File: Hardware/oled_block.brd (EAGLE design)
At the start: 30.5 x 44.5 mm, 35 parts, among them J1 EDISON_CONNECTOR_FULLMOUNTING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

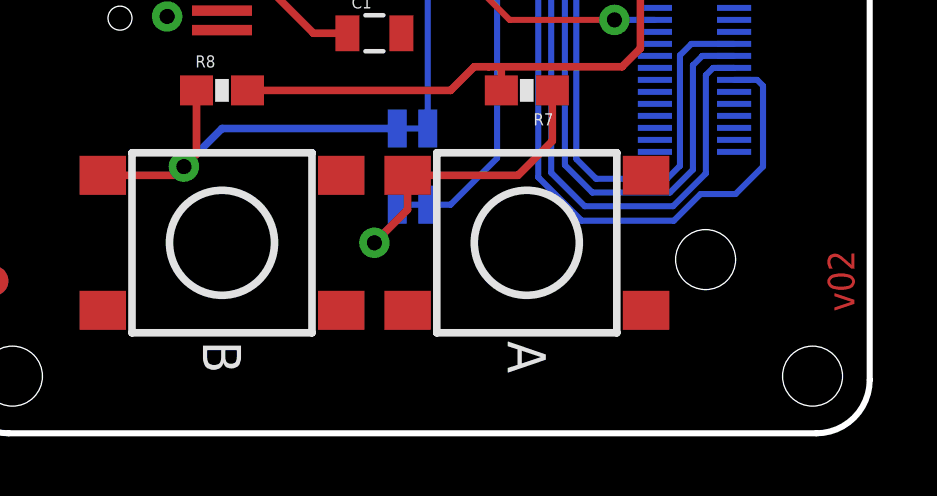
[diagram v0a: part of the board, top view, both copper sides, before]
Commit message: cleaning up some silk (v10)
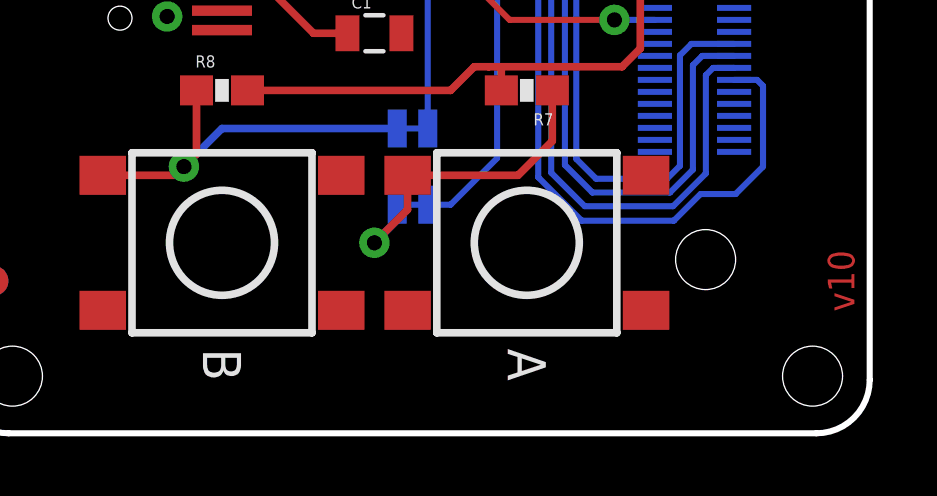
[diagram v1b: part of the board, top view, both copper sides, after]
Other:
- board text added: "v10"
- board text removed: "v02"

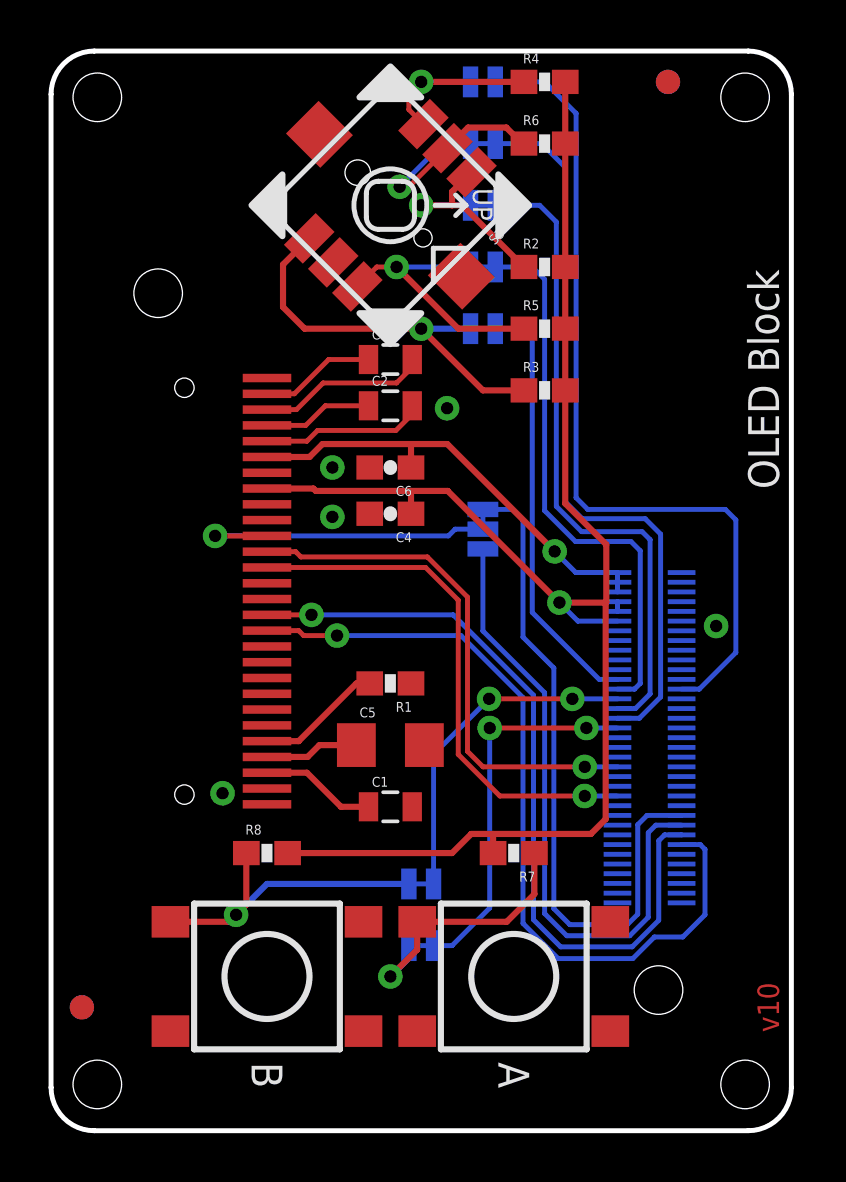
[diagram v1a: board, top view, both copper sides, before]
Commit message: Fixing button package. Silk fixes
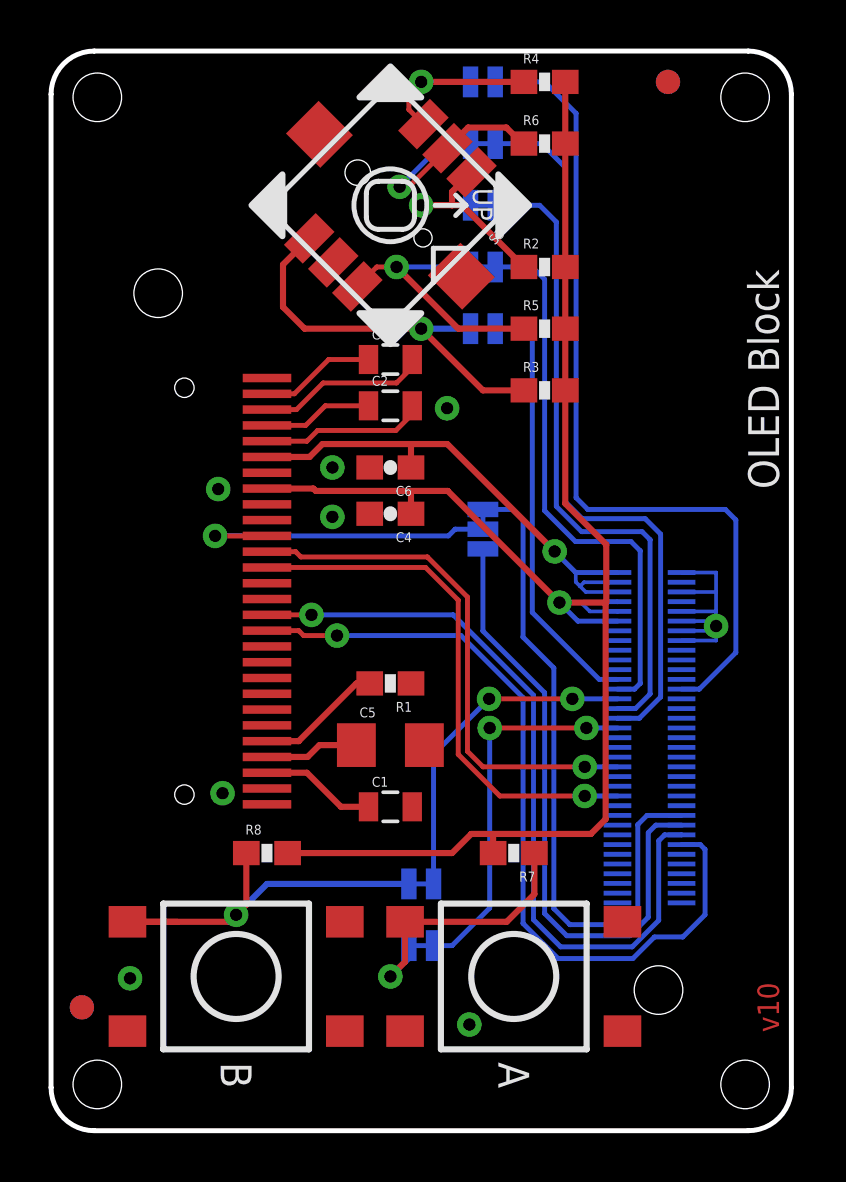
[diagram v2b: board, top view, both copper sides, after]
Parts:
- moved S2 1.27 mm to (7.62, 6.35)
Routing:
- net GND: track 0.00 -> 11.5 mm, vias 5 -> 8
- net BUT_B: track 14.0 -> 17.5 mm
- net VSYS: track 18.6 -> 21.7 mm
- net 3.3V: track 0.60 -> 3.12 mm
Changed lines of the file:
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@@
 <drawing>
 <settings>
-<setting alwaysvectorfont="no"/>
+<setting alwaysvectorfont="yes"/>
 <setting verticaltext="up"/>
 </settings>
-<grid distance="0.05" unitdist="inch" unit="inch" style="lines" multiple="1" display="yes" altdistance="0.005" altunitdist="inch" altunit="inch"/>
+<grid distance="0.025" unitdist="inch" unit="inch" style="lines" multiple="1" display="yes" altdistance="0.005" altunitdist="inch" altunit="inch"/>
 <layers>
 <layer number="1" name="Top" color="4" fill="1" visible="yes" active="yes"/>
@@
 <layer number="47" name="Measures" color="7" fill="1" visible="no" active="yes"/>
 <layer number="48" name="Document" color="7" fill="1" visible="no" active="yes"/>
-<layer number="49" name="Reference" color="7" fill="1" visible="yes" active="yes"/>
+<layer number="49" name="Reference" color="7" fill="1" visible="no" active="yes"/>
 <layer number="50" name="dxf" color="7" fill="1" visible="no" active="no"/>
 <layer number="51" name="tDocu" color="6" fill="1" visible="yes" active="yes"/>
@@
 <rectangle x1="22.098" y1="26.162" x2="30.48" y2="44.45" layer="42" rot="R180"/>
 <rectangle x1="22.098" y1="26.162" x2="30.48" y2="44.45" layer="41" rot="R180"/>
-<text x="29.21" y="6.35" size="1.016" layer="22" font="vector" ratio="15" rot="MR90" align="center">4xM2.0</text>
+<text x="29.21" y="6.35" size="1.016" layer="22" font="vector" ratio="15" rot="SMR270" align="center">4xM2.0</text>
 <text x="19.05" y="24.765" size="0.889" layer="22" font="vector" ratio="15" rot="MR90" align="bottom-center">!CS!</text>
 <text x="17.78" y="23.2664" size="0.889" layer="22" font="vector" ratio="15" rot="MR90" align="center-right">FS0</text>
 <text x="17.78" y="26.4414" size="0.889" layer="22" font="vector" ratio="15" rot="MR90" align="center-left">FS1</text>
 <text x="19.05" y="2.286" size="1.27" layer="21" font="vector" ratio="15" rot="SR270" align="center">A</text>
-<text x="8.89" y="2.286" size="1.27" layer="21" font="vector" ratio="15" rot="SR270" align="center">B</text>
+<text x="7.62" y="2.286" size="1.27" layer="21" font="vector" ratio="15" rot="SR270" align="center">B</text>
 <text x="29.972" y="26.416" size="1.27" layer="21" font="vector" ratio="15" rot="SR90">OLED Block</text>
 <text x="16.51" y="43.18" size="0.889" layer="22" font="vector" ratio="15" rot="MR180" align="center-right">L</text>
@@
 <attribute name="PROD_ID" value="SWCH-11966" x="19.05" y="6.35" size="1.778" layer="27" rot="R180" display="off"/>
 </element>
-<element name="S2" library="SparkFun-Electromechanical" package="TACTILE_SWITCH_TALL" value="Button B" x="8.89" y="6.35" rot="R180">
-<attribute name="PROD_ID" value="SWCH-11966" x="8.89" y="6.35" size="1.778" layer="27" rot="R180" display="off"/>
+<element name="S2" library="SparkFun-Electromechanical" package="TACTILE_SWITCH_TALL" value="Button B" x="7.62" y="6.35" rot="R180">
+<attribute name="PROD_ID" value="SWCH-11966" x="7.62" y="6.35" size="1.778" layer="27" rot="R180" display="off"/>
 </element>
 <element name="S3" library="SparkFun-Electromechanical" package="JOYSTICK_MINI" value="" x="13.97" y="38.1" rot="R225"/>
@@
 <signals>
 <signal name="GND">
-<polygon width="0.2032" layer="16" spacing="0.254" isolate="0.1524" orphans="yes" rank="6">
+<polygon width="0.1778" layer="16" spacing="0.254" isolate="0.1524" orphans="yes" rank="6">
 <vertex x="30.48" y="42.672"/>
 <vertex x="30.48" y="1.778" curve="-90"/>
@@
 <vertex x="28.702" y="44.45" curve="-90"/>
 </polygon>
-<polygon width="0.2032" layer="1" spacing="0.254" isolate="0.1524" orphans="yes" rank="6">
+<polygon width="0.1778" layer="1" spacing="0.254" isolate="0.1524" orphans="yes" rank="6">
 <vertex x="30.48" y="1.728" curve="-90"/>
 <vertex x="28.752" y="0"/>
@@
 <via x="7.0612" y="13.8938" extent="1-16" drill="0.508"/>
 <via x="11.5824" y="25.273" extent="1-16" drill="0.508"/>
+<wire x1="25.96" y1="22.98" x2="27.3812" y2="22.98" width="0.1524" layer="16"/>
+<wire x1="27.3812" y1="22.98" x2="27.3812" y2="22.18" width="0.1524" layer="16"/>
+<wire x1="25.96" y1="22.18" x2="27.3812" y2="22.18" width="0.1524" layer="16"/>
+<wire x1="27.3812" y1="22.18" x2="27.3812" y2="21.38" width="0.1524" layer="16"/>
+<wire x1="25.96" y1="21.38" x2="27.3812" y2="21.38" width="0.1524" layer="16"/>
+<wire x1="27.3812" y1="21.38" x2="27.3812" y2="20.7772" width="0.1524" layer="16"/>
+<wire x1="25.96" y1="20.98" x2="27.3812" y2="20.98" width="0.1524" layer="16"/>
+<wire x1="27.3812" y1="20.98" x2="27.3812" y2="20.7772" width="0.1524" layer="16"/>
+<wire x1="25.96" y1="20.58" x2="27.3812" y2="20.58" width="0.1524" layer="16"/>
+<wire x1="27.3812" y1="20.58" x2="27.3812" y2="20.7772" width="0.1524" layer="16"/>
+<wire x1="25.96" y1="20.18" x2="27.3812" y2="20.18" width="0.1524" layer="16"/>
+<wire x1="27.3812" y1="20.18" x2="27.3812" y2="20.58" width="0.1524" layer="16"/>
+<via x="3.2512" y="6.2738" extent="1-16" drill="0.508"/>
+<via x="17.2212" y="4.3688" extent="1-16" drill="0.508"/>
+<via x="6.8834" y="26.416" extent="1-16" drill="0.508"/>
 </signal>
 <signal name="VSYS">
-<wire x1="23.32" y1="22.58" x2="23.32" y2="22.18" width="0.2032" layer="16"/>
-<wire x1="23.32" y1="22.58" x2="23.32" y2="22.98" width="0.2032" layer="16"/>
 <via x="20.7338" y="23.85" extent="1-16" drill="0.508"/>
 <contactref element="J1" pad="6"/>
@@
 <wire x1="23.32" y1="22.98" x2="21.6038" y2="22.98" width="0.2032" layer="16"/>
 <wire x1="21.6038" y1="22.98" x2="20.7338" y2="23.85" width="0.2032" layer="16"/>
+<wire x1="23.32" y1="22.18" x2="22.016" y2="22.18" width="0.1524" layer="16"/>
+<wire x1="22.016" y1="22.18" x2="21.7805" y2="22.4155" width="0.1524" layer="16"/>
+<wire x1="21.7805" y1="22.4155" x2="21.6038" y2="22.5922" width="0.1524" layer="16"/>
+<wire x1="21.6038" y1="22.98" x2="21.6038" y2="22.5922" width="0.1524" layer="16"/>
+<wire x1="23.32" y1="22.58" x2="21.945" y2="22.58" width="0.1524" layer="16"/>
+<wire x1="21.945" y1="22.58" x2="21.7805" y2="22.4155" width="0.1524" layer="16"/>
 </signal>
 <signal name="3.3V">
 <wire x1="23.32" y1="21.78" x2="23.32" y2="21.7798" width="0.2032" layer="16"/>
-<wire x1="23.32" y1="21.58" x2="23.32" y2="21.38" width="0.2032" layer="16"/>
 <wire x1="23.32" y1="21.38" x2="23.32" y2="21.3798" width="0.2032" layer="16"/>
-<wire x1="23.32" y1="21.38" x2="23.32" y2="21.7798" width="0.2032" layer="16"/>
 <contactref element="J1" pad="8"/>
 <contactref element="J1" pad="10"/>
+<wire x1="23.32" y1="21.38" x2="22.181" y2="21.38" width="0.1524" layer="16"/>
+<wire x1="22.181" y1="21.38" x2="21.844" y2="21.717" width="0.1524" layer="16"/>
+<wire x1="23.32" y1="21.78" x2="21.907" y2="21.78" width="0.1524" layer="16"/>
+<wire x1="21.907" y1="21.78" x2="21.844" y2="21.717" width="0.1524" layer="16"/>
 </signal>
 <signal name="GP183_PWM3">
@@
 <wire x1="14.732" y1="10.16" x2="14.732" y2="9.652" width="0.2032" layer="16"/>
 <contactref element="R8" pad="1"/>
-<wire x1="4.915" y1="8.6" x2="5.21" y2="8.6" width="0.254" layer="1"/>
+<wire x1="3.145" y1="8.6" x2="5.21" y2="8.6" width="0.254" layer="1"/>
 <wire x1="14.732" y1="10.16" x2="8.89" y2="10.16" width="0.254" layer="16"/>
 <wire x1="8.89" y1="10.16" x2="7.62" y2="8.89" width="0.254" layer="16"/>
 <via x="7.62" y="8.89" extent="1-16" drill="0.508"/>
 <wire x1="7.62" y1="8.89" x2="7.33" y2="8.6" width="0.254" layer="1"/>
-<wire x1="7.33" y1="8.6" x2="4.915" y2="8.6" width="0.254" layer="1"/>
+<wire x1="7.33" y1="8.6" x2="3.145" y2="8.6" width="0.254" layer="1"/>
 <wire x1="8.04" y1="11.43" x2="8.04" y2="9.31" width="0.254" layer="1"/>
 <wire x1="8.04" y1="9.31" x2="7.62" y2="8.89" width="0.254" layer="1"/>
@@
 <wire x1="14.732" y1="7.112" x2="13.97" y2="6.35" width="0.254" layer="16"/>
 <via x="13.97" y="6.35" extent="1-16" drill="0.508"/>
-<wire x1="13.97" y1="6.35" x2="15.075" y2="7.455" width="0.254" layer="1"/>
-<wire x1="15.075" y1="7.455" x2="15.075" y2="8.6" width="0.254" layer="1"/>
 <wire x1="19.9" y1="11.43" x2="19.9" y2="9.74" width="0.254" layer="1"/>
 <wire x1="19.9" y1="9.74" x2="18.76" y2="8.6" width="0.254" layer="1"/>
-<wire x1="15.075" y1="8.6" x2="18.76" y2="8.6" width="0.254" layer="1"/>
+<wire x1="14.575" y1="8.6" x2="18.76" y2="8.6" width="0.254" layer="1"/>
+<wire x1="14.575" y1="8.6" x2="14.575" y2="6.955" width="0.254" layer="1"/>
+<wire x1="14.575" y1="6.955" x2="13.97" y2="6.35" width="0.254" layer="1"/>
 </signal>
 </signals>
